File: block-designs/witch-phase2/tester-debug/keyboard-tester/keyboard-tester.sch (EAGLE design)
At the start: 46 parts, among them IC1 74LVC1G17DBV, IC2 74LVC1G17DBV, IC3 74LVC1G17DBV, IC4 74LVC1G17DBV, IC5 74LVC1G17DBV, IC6 74LVC1G17DBV, IC7 74LVC1G17DBV, IC8 74LVC1G17DBV, IC9 74LVC1G17DBV

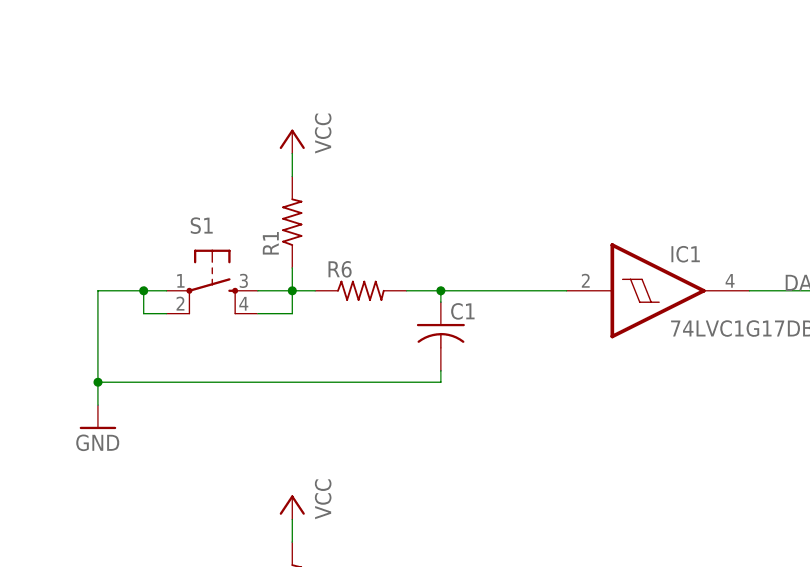
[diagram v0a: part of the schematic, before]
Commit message: move keyboard tester to new directory for test and debug boards
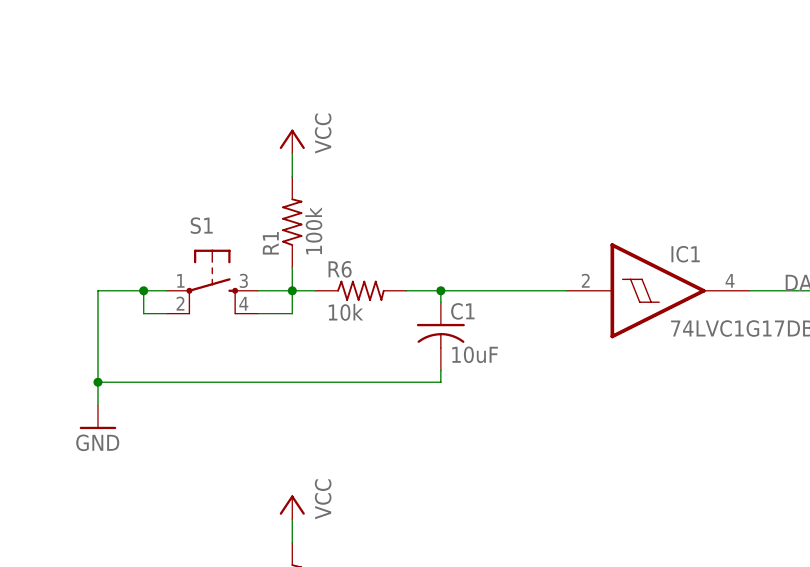
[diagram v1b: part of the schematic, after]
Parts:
- C1: value (none) -> 10uF
- R1: value (none) -> 100k
- R6: value (none) -> 10k
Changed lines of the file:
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@@
 <?xml version="1.0" encoding="utf-8"?>
 <!DOCTYPE eagle SYSTEM "eagle.dtd">
-<eagle version="7.3.0">
+<eagle version="7.6.0">
 <drawing>
 <settings>
@@
 <part name="S7" library="SparkFun-Electromechanical" deviceset="SWITCH-SPDT" device="PTH"/>
 <part name="S1" library="SparkFun-Electromechanical" deviceset="TAC_SWITCH" device="PTH"/>
-<part name="C1" library="resistor" deviceset="C-US" device="C0805"/>
-<part name="R6" library="resistor" deviceset="R-US_" device="R0805"/>
+<part name="C1" library="resistor" deviceset="C-US" device="C0805" value="10uF"/>
+<part name="R6" library="resistor" deviceset="R-US_" device="R0805" value="10k"/>
 <part name="GND1" library="supply1" deviceset="GND" device=""/>
 <part name="P+1" library="supply1" deviceset="VCC" device=""/>
-<part name="R1" library="resistor" deviceset="R-US_" device="R0805"/>
+<part name="R1" library="resistor" deviceset="R-US_" device="R0805" value="100k"/>
 <part name="IC1" library="74xx-little-us" deviceset="74*1G17" device="DBV" technology="LVC"/>
 <part name="S2" library="SparkFun-Electromechanical" deviceset="TAC_SWITCH" device="PTH"/>
